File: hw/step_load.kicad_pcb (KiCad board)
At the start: 4 copper layers, 160 x 100 mm, 206 parts, among them J1 BOOT, J2 USB_C_Receptacle_USB2.0_16P, J3 UART, J4 DC_IN, J5 DC_IN, J6 OLED, J7 OUTPUT, K1 G6K-2F-Y, K10 G6K-2F-Y, K11 G6K-2F-Y, K12 G6K-2F-Y, K13 G6K-2F-Y, K14 G6K-2F-Y, K15 G6K-2F-Y, K16 G6K-2F-Y, K2 G6K-2F-Y, K3 G6K-2F-Y, K4 G6K-2F-Y, K5 G6K-2F-Y, K6 G6K-2F-Y, K7 G6K-2F-Y, K8 G6K-2F-Y, K9 G6K-2F-Y, Q1 Si2302CDS, Q10 Si2302CDS, Q11 Si2302CDS, Q12 Si2302CDS, Q13 Si2302CDS, Q14 Si2302CDS, Q15 Si2302CDS, Q16 Si2302CDS, Q2 Si2302CDS, Q3 Si2302CDS, Q4 Si2302CDS, Q5 Si2302CDS, Q6 Si2302CDS, Q7 Si2302CDS, Q8 Si2302CDS, Q9 Si2302CDS, SW1 RST, SW2 RST, SW3 RST, SW4 RST, U1 LM35DZ, U2 LM35DZ, U3 AZ1117-3.3, U4 ESP32-C3-WROOM-02, U5 TCA9535PWR

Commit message: pcb completed
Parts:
- added R79: 1K, Resistor_SMD:R_0603_1608Metric, F.Cu at (93.5, 120.5)
- added R80: 1K, Resistor_SMD:R_0603_1608Metric, F.Cu at (95.0, 120.5)
- added R81: 1K, Resistor_SMD:R_0603_1608Metric, F.Cu at (96.5, 120.5)
- added R82: 1K, Resistor_SMD:R_0603_1608Metric, F.Cu at (95.8, 73.7)
- added R83: 1K, Resistor_SMD:R_0603_1608Metric, F.Cu at (94.3, 73.7)
- added R84: 1K, Resistor_SMD:R_0603_1608Metric, F.Cu at (92.8, 73.7)
- D11, D12, D13, D14, D19, D20, D21, D22, D27, D28, D29, D30, D35, D36, D37, D38, D5, D6: footprint Diode_SMD:D_SOD-323_HandSoldering -> Diode_SMD:D_SOD-323
- moved J7 0.54 mm to (246.0, 82.4)
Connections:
- C4 pad 1: +3.3V -> VIN
- C5 pad 1: +3.3V -> VIN
- U1 pad 1: +3.3V -> VIN
- U1 pad 2: TEMP_AMB -> Net-(U1-Signal)
- U2 pad 1: +3.3V -> VIN
- U2 pad 2: TEMP_RES -> Net-(U2-Signal)
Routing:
- net VIN: track 7.52 -> 220.6 mm, vias 0 -> 2
- net Net-(U2-Signal): track 0.00 -> 153.3 mm, vias 0 -> 1
- net TEMP_RES: track 160.4 -> 8.26 mm, vias 1 -> 0
- net +3.3V: track 72.3 -> 10.3 mm
- net GND: track 217.7 -> 233.9 mm
- net Net-(U1-Signal): track 0.00 -> 3.99 mm
- net TEMP_AMB: track 44.4 -> 40.9 mm
- net Net-(R83-Pad1): track 0.00 -> 1.51 mm
- net Net-(R80-Pad1): track 0.00 -> 1.49 mm
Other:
- board text added: "6.25Ω - 100Ω 4 W/R"
- board text removed: "6.25Ω - 100Ω 4 Wmax Per"

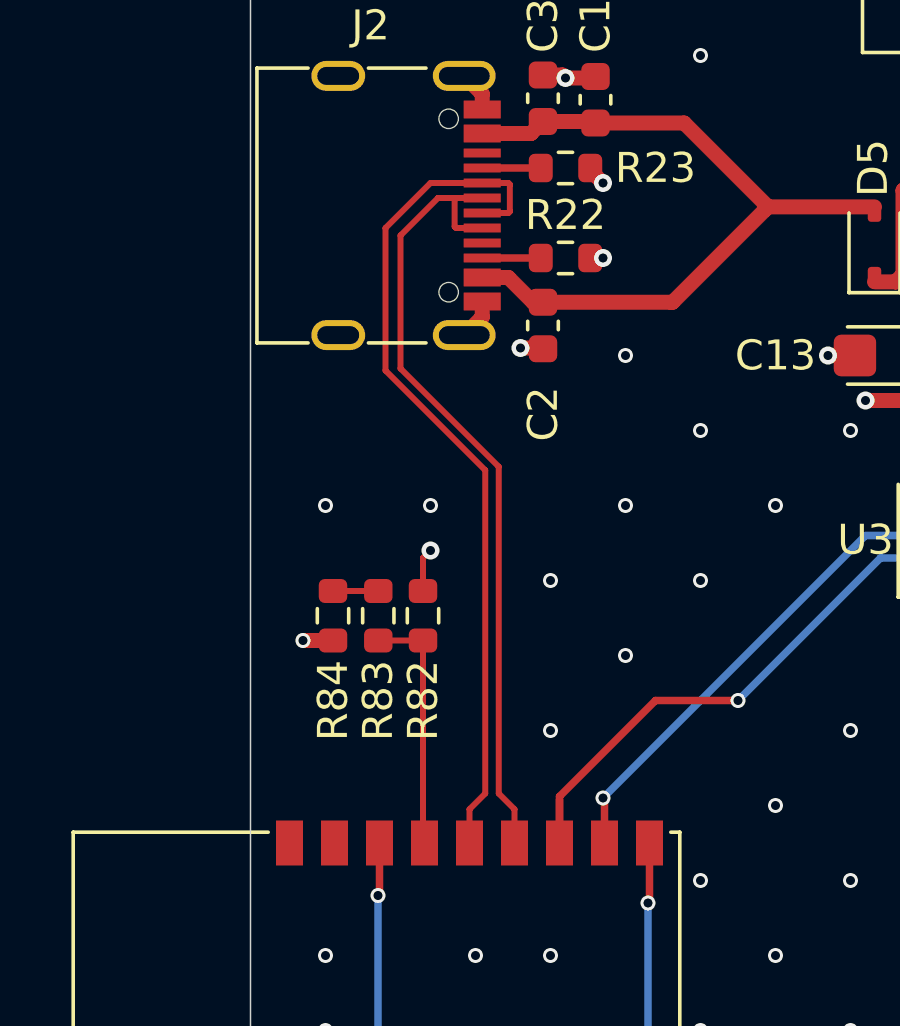
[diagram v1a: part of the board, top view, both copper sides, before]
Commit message: Swapt USB+ (A6 & B6) and USB- (A7 & B7) connection, fix the Device Unknown issue
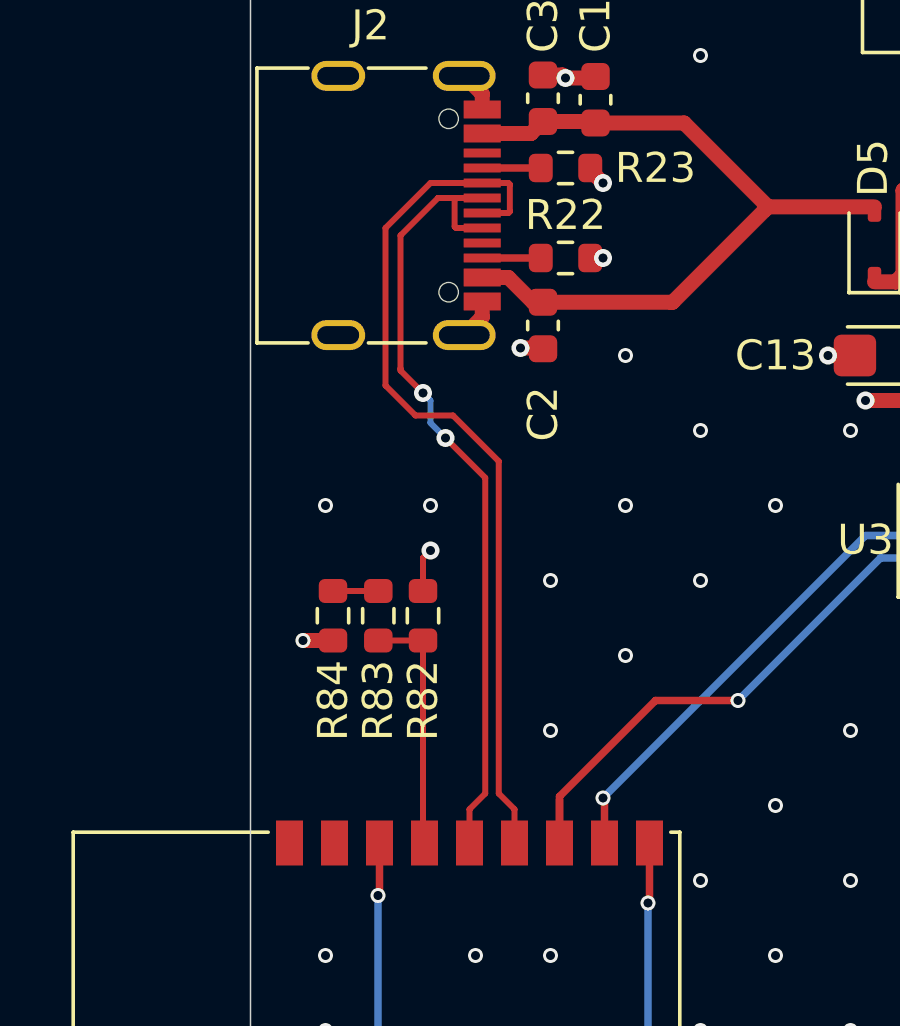
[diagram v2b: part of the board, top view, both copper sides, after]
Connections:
- J2 pad A6: USB_ESP- -> USB_ESP+
- J2 pad A7: USB_ESP+ -> USB_ESP-
- J2 pad B6: USB_ESP- -> USB_ESP+
- J2 pad B7: USB_ESP+ -> USB_ESP-
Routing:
- net USB_ESP-: track 27.0 -> 29.6 mm
- net USB_ESP+: track 28.7 -> 26.8 mm, vias 0 -> 2
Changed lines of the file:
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@@
 		(sheetname "/RELAYS/")
 		(sheetfile "relays.kicad_sch")
-		(attr smd)
+		(attr smd exclude_from_bom dnp)
 		(fp_line
 			(start -3.34 0.8)
@@
 		(sheetname "/RELAYS/")
 		(sheetfile "relays.kicad_sch")
-		(attr smd)
+		(attr smd exclude_from_bom dnp)
 		(fp_line
 			(start -3.34 0.8)
@@
 		(sheetname "/RELAYS/")
 		(sheetfile "relays.kicad_sch")
-		(attr smd)
+		(attr smd exclude_from_bom dnp)
 		(fp_line
 			(start -3.34 0.8)
@@
 			(size 0.3 1.24)
 			(layers "F.Cu" "F.Mask" "F.Paste")
-			(net 63 "USB_ESP-")
+			(net 60 "USB_ESP+")
 			(pinfunction "D+")
 			(pintype "bidirectional")
@@
 			(size 0.3 1.24)
 			(layers "F.Cu" "F.Mask" "F.Paste")
-			(net 60 "USB_ESP+")
+			(net 63 "USB_ESP-")
 			(pinfunction "D-")
 			(pintype "bidirectional")
@@
 			(size 0.3 1.24)
 			(layers "F.Cu" "F.Mask" "F.Paste")
-			(net 63 "USB_ESP-")
+			(net 60 "USB_ESP+")
 			(pinfunction "D+")
 			(pintype "bidirectional")
@@
 			(size 0.3 1.24)
 			(layers "F.Cu" "F.Mask" "F.Paste")
-			(net 60 "USB_ESP+")
+			(net 63 "USB_ESP-")
 			(pinfunction "D-")
 			(pintype "bidirectional")
@@
 		(sheetname "/RELAYS/")
 		(sheetfile "relays.kicad_sch")
-		(attr smd)
+		(attr smd exclude_from_bom dnp)
 		(fp_line
 			(start 3.36 5.1)
@@
 		(sheetname "/RELAYS/")
 		(sheetfile "relays.kicad_sch")
-		(attr smd)
+		(attr smd exclude_from_bom dnp)
 		(fp_line
 			(start 3.36 5.1)
@@
 		(sheetname "/RELAYS/")
 		(sheetfile "relays.kicad_sch")
-		(attr smd)
+		(attr smd exclude_from_bom dnp)
 		(fp_line
 			(start -3.34 0.8)
@@
 		(sheetname "/RELAYS/")
 		(sheetfile "relays.kicad_sch")
-		(attr smd)
+		(attr smd exclude_from_bom dnp)
 		(fp_line
 			(start -3.34 0.8)
@@
 		(sheetname "/RELAYS/")
 		(sheetfile "relays.kicad_sch")
-		(attr smd)
+		(attr smd exclude_from_bom dnp)
 		(fp_line
 			(start 3.36 5.1)
@@
 		(sheetname "/")
 		(sheetfile "step_load.kicad_sch")
-		(attr smd)
+		(attr smd exclude_from_bom dnp)
 		(fp_line
 			(start -1.85 3.41)
@@
 		(sheetname "/RELAYS/")
 		(sheetfile "relays.kicad_sch")
-		(attr smd)
+		(attr smd exclude_from_bom dnp)
 		(fp_line
 			(start -3.34 0.8)
@@
 		(sheetname "/RELAYS/")
 		(sheetfile "relays.kicad_sch")
-		(attr smd)
+		(attr smd exclude_from_bom dnp)
 		(fp_line
 			(start -3.34 0.8)
@@
 		(sheetname "/RELAYS/")
 		(sheetfile "relays.kicad_sch")
-		(attr smd)
+		(attr smd exclude_from_bom dnp)
 		(fp_line
 			(start 3.36 5.1)
@@
 		(sheetname "/RELAYS/")
 		(sheetfile "relays.kicad_sch")
-		(attr smd)
+		(attr smd exclude_from_bom dnp)
 		(fp_line
 			(start 3.36 5.1)
@@
 		(sheetname "/RELAYS/")
 		(sheetfile "relays.kicad_sch")
-		(attr smd)
+		(attr smd exclude_from_bom dnp)
 		(fp_line
 			(start 3.36 5.1)
@@
 		(sheetname "/RELAYS/")
 		(sheetfile "relays.kicad_sch")
-		(attr smd)
+		(attr smd exclude_from_bom dnp)
 		(fp_line
 			(start -3.34 0.8)
@@
 		(sheetname "/RELAYS/")
 		(sheetfile "relays.kicad_sch")
-		(attr smd)
+		(attr smd exclude_from_bom dnp)
 		(fp_line
 			(start 3.36 5.1)
@@
 		(sheetname "/RELAYS/")
 		(sheetfile "relays.kicad_sch")
-		(attr smd)
+		(attr smd exclude_from_bom dnp)
 		(fp_line
 			(start 3.36 5.1)
@@
 	)
 	(segment
-		(start 98.646 60.201)
-		(end 98.597 60.25)
+		(start 97.725 59.75)
+		(end 96.853 59.75)
 		(width 0.2)
 		(layer "F.Cu")
@@
 	)
 	(segment
-		(start 97.725 59.25)
-		(end 98.597 59.25)
+		(start 97.3 80.124999)
+		(end 97.825 79.599999)
 		(width 0.2)
 		(layer "F.Cu")
@@
 	)
 	(segment
-		(start 97.825 68.825)
-		(end 94.5 65.5)
+		(start 96.853 59.75)
+		(end 96.804 59.799)
 		(width 0.2)
 		(layer "F.Cu")
@@
 	)
 	(segment
-		(start 94.5 65.5)
-		(end 94.5 60.75)
+		(start 96.804 60.701)
+		(end 96.853 60.75)
 		(width 0.2)
 		(layer "F.Cu")
@@
 	)
 	(segment
-		(start 98.597 59.25)
-		(end 98.646 59.299)
+		(start 95 65.5)
+		(end 95.75 66.25)
 		(width 0.2)
 		(layer "F.Cu")
@@
 	)
 	(segment
-		(start 97.3 80.124999)
-		(end 97.825 79.599999)
+		(start 96.853 60.75)
+		(end 97.725 60.75)
 		(width 0.2)
 		(layer "F.Cu")
@@
 	)
 	(segment
-		(start 97.3 81.25)
-		(end 97.3 80.124999)
+		(start 97.825 69.075)
+		(end 96.5 67.75)
 		(width 0.2)
 		(layer "F.Cu")
@@
 	)
 	(segment
-		(start 98.646 59.299)
-		(end 98.646 60.201)
+		(start 95 61)
+		(end 96.25 59.75)
 		(width 0.2)
 		(layer "F.Cu")
@@
 	)
 	(segment
-		(start 94.5 60.75)
-		(end 96 59.25)
+		(start 95 65.4329)
+		(end 95 61)
 		(width 0.2)
 		(layer "F.Cu")
@@
 	(segment
 		(start 97.825 79.599999)
-		(end 97.825 68.825)
+		(end 97.825 69.075)
 		(width 0.2)
 		(layer "F.Cu")
@@
 	)
 	(segment
-		(start 98.597 60.25)
-		(end 97.725 60.25)
+		(start 96.804 59.799)
+		(end 96.804 60.701)
 		(width 0.2)
 		(layer "F.Cu")
@@
 	)
 	(segment
-		(start 96 59.25)
-		(end 97.725 59.25)
+		(start 96.25 59.75)
+		(end 96.853 59.75)
+		(width 0.2)
+		(layer "F.Cu")
+		(net 60)
+	)
+	(segment
+		(start 95 65.4329)
+		(end 95 65.5)
 		(width 0.2)
 		(layer "F.Cu")
@@
 	)
 	(segment
+		(start 97.3 81.25)
+		(end 97.3 80.124999)
+		(width 0.2)
+		(layer "F.Cu")
+		(net 60)
+	)
+	(via
+		(at 96.5 67.75)
+		(size 0.6)
+		(drill 0.3)
+		(layers "F.Cu" "B.Cu")
+		(net 60)
+	)
+	(via
+		(at 95.75 66.25)
+		(size 0.6)
+		(drill 0.3)
+		(layers "F.Cu" "B.Cu")
+		(net 60)
+	)
+	(segment
+		(start 96 66.5)
+		(end 96 67.25)
+		(width 0.2)
+		(layer "B.Cu")
+		(net 60)
+	)
+	(segment
+		(start 95.75 66.25)
+		(end 96 66.5)
+		(width 0.2)
+		(layer "B.Cu")
+		(net 60)
+	)
+	(segment
+		(start 96 67.25)
+		(end 96.5 67.75)
+		(width 0.2)
+		(layer "B.Cu")
+		(net 60)
+	)
+	(segment
 		(start 97.725 58.75)
 		(end 99.675 58.75)
@@
 	)
 	(segment
-		(start 98.275 79.599999)
-		(end 98.275 68.7079)
+		(start 94.5 66.000001)
+		(end 95.499999 67)
 		(width 0.2)
 		(layer "F.Cu")
@@
 	)
 	(segment
-		(start 98.8 81.25)
-		(end 98.8 80.124999)
+		(start 98.646 60.201)
+		(end 98.597 60.25)
 		(width 0.2)
 		(layer "F.Cu")
@@
 	)
 	(segment
-		(start 97.725 59.75)
-		(end 96.853 59.75)
+		(start 97.725 59.25)
+		(end 98.597 59.25)
 		(width 0.2)
 		(layer "F.Cu")
@@
 	)
 	(segment
-		(start 96.853 59.75)
-		(end 96.804 59.799)
+		(start 98.8 80.124999)
+		(end 98.8 81.25)
 		(width 0.2)
 		(layer "F.Cu")
@@
 	)
 	(segment
-		(start 96.804 60.701)
-		(end 96.853 60.75)
+		(start 96 59.25)
+		(end 94.5 60.75)
 		(width 0.2)
 		(layer "F.Cu")
@@
 	)
 	(segment
-		(start 96.853 60.75)
-		(end 97.725 60.75)
+		(start 94.5 60.75)
+		(end 94.5 66.000001)
 		(width 0.2)
 		(layer "F.Cu")
@@
 	)
 	(segment
-		(start 98.275 68.7079)
-		(end 95 65.4329)
+		(start 97.725 59.25)
+		(end 96 59.25)
 		(width 0.2)
 		(layer "F.Cu")
@@
 	)
 	(segment
-		(start 95 61)
-		(end 96.25 59.75)
+		(start 98.275 68.525)
+		(end 98.275 79.599999)
 		(width 0.2)
 		(layer "F.Cu")
@@
 	)
 	(segment
-		(start 95 65.4329)
-		(end 95 61)
+		(start 98.597 59.25)
+		(end 98.646 59.299)
 		(width 0.2)
 		(layer "F.Cu")
@@
 	)
 	(segment
-		(start 96.804 59.799)
-		(end 96.804 60.701)
+		(start 96.75 67)
+		(end 98.275 68.525)
 		(width 0.2)
 		(layer "F.Cu")
@@
 	)
 	(segment
-		(start 98.8 80.124999)
-		(end 98.275 79.599999)
+		(start 98.646 59.299)
+		(end 98.646 60.201)
 		(width 0.2)
 		(layer "F.Cu")
@@
 	)
 	(segment
-		(start 96.25 59.75)
-		(end 96.853 59.75)
+		(start 95.499999 67)
+		(end 96.75 67)
+		(width 0.2)
+		(layer "F.Cu")
+		(net 63)
+	)
+	(segment
+		(start 98.597 60.25)
+		(end 97.725 60.25)
+		(width 0.2)
+		(layer "F.Cu")
+		(net 63)
+	)
+	(segment
+		(start 98.275 79.599999)
+		(end 98.8 80.124999)
 		(width 0.2)
 		(layer "F.Cu")
